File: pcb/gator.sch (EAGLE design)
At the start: 69 parts, among them J2 POWER_JACKPTH

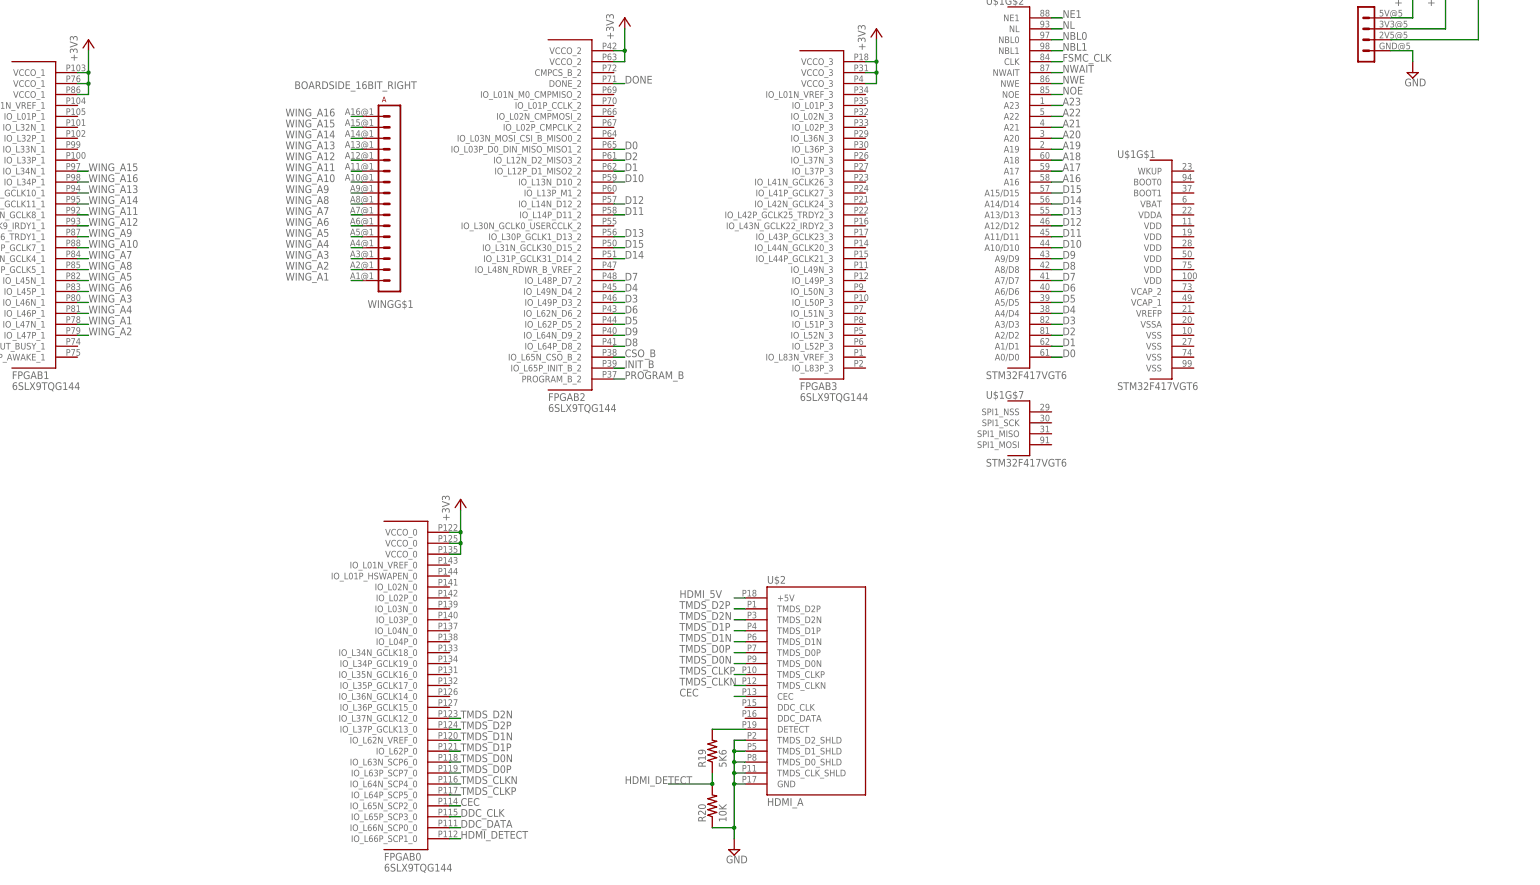
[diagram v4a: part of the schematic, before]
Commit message: Added SDRAM part and connected it to FPGA
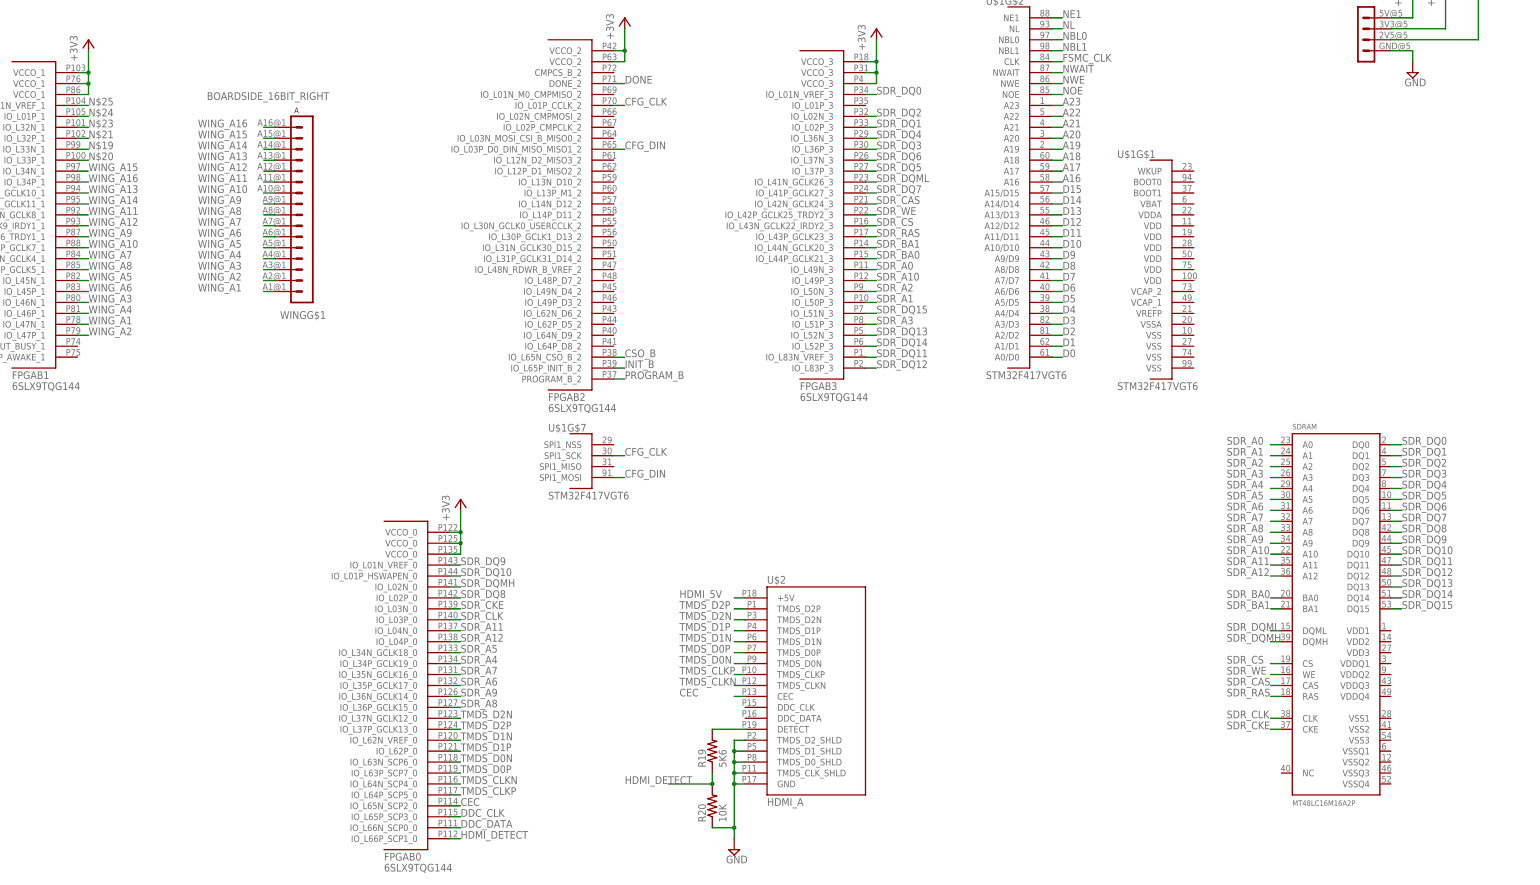
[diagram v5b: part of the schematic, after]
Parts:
- added SDRAM: MT48LC16M16A2P, gator:MT48LC16M16A2P
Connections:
- new net CFG_CLK: FPGAB2.IO_L01P_CCLK_2, U$1G$7.SPI1_SCK
- new net CFG_DIN: FPGAB2.IO_L03P_D0_DIN_MISO_MISO1_2, U$1G$7.SPI1_MOSI
- new net N$19: FPGAB1.IO_L33N_1
- new net N$20: FPGAB1.IO_L33P_1
- new net N$21: FPGAB1.IO_L32P_1
- new net N$23: FPGAB1.IO_L32N_1
- new net N$24: FPGAB1.IO_L01P_1
- new net N$25: FPGAB1.IO_L01N_VREF_1
- new net SDR_A0: FPGAB3.IO_L49N_3, SDRAM.A0
- new net SDR_A1: FPGAB3.IO_L50P_3, SDRAM.A1
- new net SDR_A10: FPGAB3.IO_L49P_3, SDRAM.A10
- new net SDR_A11: FPGAB0.IO_L04N_0, SDRAM.A11
- new net SDR_A12: FPGAB0.IO_L04P_0, SDRAM.A12
- new net SDR_A2: FPGAB3.IO_L50N_3, SDRAM.A2
- new net SDR_A3: FPGAB3.IO_L51P_3, SDRAM.A3
- new net SDR_A4: FPGAB0.IO_L34P_GCLK19_0, SDRAM.A4
- new net SDR_A5: FPGAB0.IO_L34N_GCLK18_0, SDRAM.A5
- new net SDR_A6: FPGAB0.IO_L35P_GCLK17_0, SDRAM.A6
- new net SDR_A7: FPGAB0.IO_L35N_GCLK16_0, SDRAM.A7
- new net SDR_A8: FPGAB0.IO_L36P_GCLK15_0, SDRAM.A8
- new net SDR_A9: FPGAB0.IO_L36N_GCLK14_0, SDRAM.A9
- new net SDR_BA0: FPGAB3.IO_L44P_GCLK21_3, SDRAM.BA0
- new net SDR_BA1: FPGAB3.IO_L44N_GCLK20_3, SDRAM.BA1
- new net SDR_CAS: FPGAB3.IO_L42N_GCLK24_3, SDRAM.CAS
- new net SDR_CKE: FPGAB0.IO_L03N_0, SDRAM.CKE
- new net SDR_CLK: FPGAB0.IO_L03P_0, SDRAM.CLK
- new net SDR_CS: FPGAB3.IO_L43N_GCLK22_IRDY2_3, SDRAM.CS
- new net SDR_DQ0: FPGAB3.IO_L01N_VREF_3, SDRAM.DQ0
- new net SDR_DQ1: FPGAB3.IO_L02P_3, SDRAM.DQ1
- new net SDR_DQ10: FPGAB0.IO_L01P_HSWAPEN_0, SDRAM.DQ10
- new net SDR_DQ11: FPGAB3.IO_L83N_VREF_3, SDRAM.DQ11
- new net SDR_DQ12: FPGAB3.IO_L83P_3, SDRAM.DQ12
- new net SDR_DQ13: FPGAB3.IO_L52N_3, SDRAM.DQ13
- new net SDR_DQ14: FPGAB3.IO_L52P_3, SDRAM.DQ14
- new net SDR_DQ15: FPGAB3.IO_L51N_3, SDRAM.DQ15
- new net SDR_DQ2: FPGAB3.IO_L02N_3, SDRAM.DQ2
- new net SDR_DQ3: FPGAB3.IO_L36P_3, SDRAM.DQ3
- new net SDR_DQ4: FPGAB3.IO_L36N_3, SDRAM.DQ4
- new net SDR_DQ5: FPGAB3.IO_L37P_3, SDRAM.DQ5
- new net SDR_DQ6: FPGAB3.IO_L37N_3, SDRAM.DQ6
- new net SDR_DQ7: FPGAB3.IO_L41P_GCLK27_3, SDRAM.DQ7
- new net SDR_DQ8: FPGAB0.IO_L02P_0, SDRAM.DQ8
- new net SDR_DQ9: FPGAB0.IO_L01N_VREF_0, SDRAM.DQ9
- new net SDR_DQMH: FPGAB0.IO_L02N_0, SDRAM.DQMH
- new net SDR_DQML: FPGAB3.IO_L41N_GCLK26_3, SDRAM.DQML
- new net SDR_RAS: FPGAB3.IO_L43P_GCLK23_3, SDRAM.RAS
- new net SDR_WE: FPGAB3.IO_L42P_GCLK25_TRDY2_3, SDRAM.WE
- net D0: no longer FPGAB2.IO_L03P_D0_DIN_MISO_MISO1_2
- net D1: no longer FPGAB2.IO_L12P_D1_MISO2_2
- net D10: no longer FPGAB2.IO_L13N_D10_2
- net D11: no longer FPGAB2.IO_L14P_D11_2
- net D12: no longer FPGAB2.IO_L14N_D12_2
- net D13: no longer FPGAB2.IO_L30P_GCLK1_D13_2
- net D14: no longer FPGAB2.IO_L31P_GCLK31_D14_2
- net D15: no longer FPGAB2.IO_L31N_GCLK30_D15_2
- net D2: no longer FPGAB2.IO_L12N_D2_MISO3_2
- net D3: no longer FPGAB2.IO_L49P_D3_2
- net D4: no longer FPGAB2.IO_L49N_D4_2
- net D5: no longer FPGAB2.IO_L62P_D5_2
- net D6: no longer FPGAB2.IO_L62N_D6_2
- net D7: no longer FPGAB2.IO_L48P_D7_2
- net D8: no longer FPGAB2.IO_L64P_D8_2
- net D9: no longer FPGAB2.IO_L64N_D9_2
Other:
- moved on the sheet: U$1G$7, WINGG$1

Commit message: Connected FSMC; 8-bit Papilio wing
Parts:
- removed WING: BOARDSIDE_16BIT_RIGHT, GadgetFactory_Pub:BOARDSIDE_16BIT_RIGHT
- added U$3: WING8, Papilio:WING8
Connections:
- removed net +5V: WINGG$2.5V, WINGG$3.5V
- removed net WING_A1: FPGAB1.IO_L47N_1, WINGG$1.A1
- removed net WING_A10: FPGAB1.IO_L42P_GCLK7_1, WINGG$1.A10
- removed net WING_A11: FPGAB1.IO_L41N_GCLK8_1, WINGG$1.A11
- removed net WING_A12: FPGAB1.IO_L41P_GCLK9_IRDY1_1, WINGG$1.A12
- removed net WING_A13: FPGAB1.IO_L40N_GCLK10_1, WINGG$1.A13
- removed net WING_A14: FPGAB1.IO_L40P_GCLK11_1, WINGG$1.A14
- removed net WING_A15: FPGAB1.IO_L34N_1, WINGG$1.A15
- removed net WING_A16: FPGAB1.IO_L34P_1, WINGG$1.A16
- removed net WING_A2: FPGAB1.IO_L47P_1, WINGG$1.A2
- removed net WING_A3: FPGAB1.IO_L46N_1, WINGG$1.A3
- removed net WING_A4: FPGAB1.IO_L46P_1, WINGG$1.A4
- removed net WING_A5: FPGAB1.IO_L45N_1, WINGG$1.A5
- removed net WING_A6: FPGAB1.IO_L45P_1, WINGG$1.A6
- removed net WING_A7: FPGAB1.IO_L43N_GCLK4_1, WINGG$1.A7
- removed net WING_A8: FPGAB1.IO_L43P_GCLK5_1, WINGG$1.A8
- removed net WING_A9: FPGAB1.IO_L42N_GCLK6_TRDY1_1, WINGG$1.A9
- new net N$26: FPGAB1.IO_L34N_1, U$3.1
- new net N$27: FPGAB1.IO_L34P_1, U$3.2
- net +3V3: no longer WINGG$2.3V3, WINGG$3.3V3
- net A16: now also FPGAB2.IO_L49P_D3_2
- net A17: now also FPGAB2.IO_L49N_D4_2
- net A18: now also FPGAB2.IO_L62P_D5_2
- net A19: now also FPGAB1.IO_L46P_1
- net A20: now also FPGAB1.IO_L46N_1
- net A21: now also FPGAB1.IO_L47P_1
- net A22: now also FPGAB1.IO_L47N_1
- net A23: now also FPGAB1.IO_L45N_1
- net D0: now also FPGAB2.IO_L62N_D6_2
- net D1: now also FPGAB2.IO_L64P_D8_2
- net D10: now also FPGAB2.IO_L30P_GCLK1_D13_2
- net D11: now also FPGAB2.IO_L30N_GCLK0_USERCCLK_2
- net D12: now also FPGAB2.IO_L31P_GCLK31_D14_2
- net D13: now also FPGAB2.IO_L31N_GCLK30_D15_2
- net D14: now also FPGAB2.IO_L48P_D7_2
- net D15: now also FPGAB2.IO_L48N_RDWR_B_VREF_2
- net D2: now also FPGAB1.IO_L40P_GCLK11_1
- net D3: now also FPGAB1.IO_L40N_GCLK10_1
- net D4: now also FPGAB2.IO_L12P_D1_MISO2_2
- net D5: now also FPGAB2.IO_L12N_D2_MISO3_2
- net D6: now also FPGAB2.IO_L13P_M1_2
- net D7: now also FPGAB2.IO_L13N_D10_2
- net D8: now also FPGAB2.IO_L14P_D11_2
- net D9: now also FPGAB2.IO_L14N_D12_2
- net GND: no longer WINGG$2.GND, WINGG$3.GND
- net INIT_B: no longer U$1G$9.PB0
- net N$19: now also FPGAB1.IO_L01N_VREF_1, U$3.7; no longer FPGAB1.IO_L33N_1
- net N$20: now also FPGAB1.IO_L01P_1, U$3.8; no longer FPGAB1.IO_L33P_1
- net N$21: now also FPGAB1.IO_L32N_1, U$3.5; no longer FPGAB1.IO_L32P_1
- net N$23: now also FPGAB1.IO_L32P_1, U$3.6; no longer FPGAB1.IO_L32N_1
- net N$24: now also FPGAB1.IO_L33N_1, U$3.3; no longer FPGAB1.IO_L01P_1
- net N$25: now also FPGAB1.IO_L33P_1, U$3.4; no longer FPGAB1.IO_L01N_VREF_1
- net NBL0: now also FPGAB1.IO_L43N_GCLK4_1
- net NBL1: now also FPGAB1.IO_L45P_1
- net NE1: now also FPGAB1.IO_L42N_GCLK6_TRDY1_1
- net NL: now also FPGAB1.IO_L43P_GCLK5_1
- net NOE: now also FPGAB1.IO_L41P_GCLK9_IRDY1_1
- net NWAIT: now also FPGAB1.IO_L42P_GCLK7_1
- net NWE: now also FPGAB1.IO_L41N_GCLK8_1
- net PROGRAM_B: no longer U$1G$9.PB1
- net VCC/2: no longer WINGG$2.2V5, WINGG$3.2V5

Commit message: Cleaned up power supplies and connected usb and micro sd
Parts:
- removed C18, C20: 100n, SparkFun-Passives:CAP0603-CAP
- removed C19: 2.2u, SparkFun-Passives:CAP0603-CAP
- removed TLV1117-25CDCYR: (no value), microbuilder:LM1117SOT223-REFLOW
- removed U$3: WING8, Papilio:WING8
- added R21, R22: 22, SparkFun-Passives:RESISTOR0603-RES
- added R23: 10K, SparkFun-Passives:RESISTOR0603-RES
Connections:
- removed net N$23: FPGAB1.IO_L32P_1, U$3.6
- removed net N$24: FPGAB1.IO_L33N_1, U$3.3
- removed net N$25: FPGAB1.IO_L33P_1, U$3.4
- removed net N$26: FPGAB1.IO_L34N_1, U$3.1
- removed net N$27: FPGAB1.IO_L34P_1, U$3.2
- removed net TCLK/SWCLK: JTAG.9
- removed net VCC/2: C19.1, C20.1, TLV1117-25CDCYR.OUT
- new net SPI_MISO: FPGAB2.IO_L02N_CMPMOSI_2, U$1G$7.SPI1_MISO
- net +3V3: now also SDRAM.VDD1, SDRAM.VDD2, SDRAM.VDD3, SDRAM.VDDQ1, SDRAM.VDDQ2, SDRAM.VDDQ3, SDRAM.VDDQ4
- net GND: now also SDRAM.VSS1, SDRAM.VSS2, SDRAM.VSS3, SDRAM.VSSQ1, SDRAM.VSSQ2, SDRAM.VSSQ3, SDRAM.VSSQ4, U$1G$1.VSS@10, U$1G$1.VSS@27, U$1G$1.VSS@74, U$1G$1.VSS@99, U$1G$1.VSSA; no longer C18.2, C19.2, C20.2, TLV1117-25CDCYR.ADJ
- net N$1: now also R21.2; no longer USBA.D+
- net N$19: now also R21.1, USBA.D+; no longer FPGAB1.IO_L01N_VREF_1, U$3.7
- net N$2: now also R22.2; no longer USBA.D-
- net N$20: now also R22.1, USBA.D-; no longer FPGAB1.IO_L01P_1, U$3.8
- net N$21: now also MIC5219-5.0YM1.EN, R23.1; no longer FPGAB1.IO_L32N_1, U$3.5
- net TCK/SWCLK: now also JTAG.9
- net USB_EN: no longer MIC5219-5.0YM1.EN
- net V+: now also R23.2; no longer C18.1, TLV1117-25CDCYR.IN
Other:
- moved on the sheet: U$1G$9

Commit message: Added HDMI termination, oscillators, improved routing
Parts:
- added C18, C19: 20p, SparkFun-Passives:CAP0603-CAP
- added OSC_50M: OSCILLATOR5X3-PIN1-INDICATED, SparkFun-FreqCtrl:OSCILLATOR5X3-PIN1-INDICATED
- added R24, R25: 10K, SparkFun-Passives:RESISTOR0603-RES
- added R26: 2K2, SparkFun-Passives:RESISTOR0603-RES
- added R27, R28: 51, SparkFun-Passives:RESISTOR-ARRAY0603-ARV
- added Y1: 12MHz, SparkFun-FreqCtrl:CRYSTALHC49US
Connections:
- new net FPGA_CLK1: FPGAB1.IO_L34N_1, U$1G$8.MCO1
- new net FPGA_CLK2: FPGAB1.IO_L34P_1
- new net N$29: C18.1, U$1G$8.OSC_IN, Y1.2
- new net N$30: C19.1, U$1G$8.OSC_OUT, Y1.1
- new net N$31: OSC_50M.EN, R26.1
- new net SD_DETECT: MICROSD.SHIELD@2, R24.1, U$1G$9.PC7
- net +3V3: now also OSC_50M.VCC, R24.2, R26.2; no longer FPGAB0.VCCO_0@000, FPGAB0.VCCO_0@001, FPGAB0.VCCO_0@002, FPGAB1.VCCO_1@000, FPGAB1.VCCO_1@001, FPGAB1.VCCO_1@002, FPGAB2.VCCO_2@000, FPGAB2.VCCO_2@001, FPGAB3.VCCO_3@000, FPGAB3.VCCO_3@001, FPGAB3.VCCO_3@002, FPGABVCCAUX.VCCAUX@000, FPGABVCCAUX.VCCAUX@001, FPGABVCCAUX.VCCAUX@002, FPGABVCCAUX.VCCAUX@003, FPGABVCCAUX.VCCAUX@004
- net 50MHZ_OSC: now also OSC_50M.OUT
- net GND: now also C18.2, C19.2, OSC_50M.GND
- net TMDS_CLKN: now also R27A.1
- net TMDS_CLKP: now also R27B.1
- net TMDS_D0N: now also R27C.1
- net TMDS_D0P: now also R27D.1
- net TMDS_D1N: now also R28A.1
- net TMDS_D1P: now also R28B.1
- net TMDS_D2N: now also R28C.1
- net TMDS_D2P: now also R28D.1
- net USB_EN: now also R25.1, U$1G$9.PC6; no longer U$1G$5.USB_EN_ID
- net V+: now also R25.2
- net VCCIO: now also FPGAB0.VCCO_0@000, FPGAB0.VCCO_0@001, FPGAB0.VCCO_0@002, FPGAB1.VCCO_1@000, FPGAB1.VCCO_1@001, FPGAB1.VCCO_1@002, FPGAB2.VCCO_2@000, FPGAB2.VCCO_2@001, FPGAB3.VCCO_3@000, FPGAB3.VCCO_3@001, FPGAB3.VCCO_3@002, FPGABVCCAUX.VCCAUX@000, FPGABVCCAUX.VCCAUX@001, FPGABVCCAUX.VCCAUX@002, FPGABVCCAUX.VCCAUX@003, FPGABVCCAUX.VCCAUX@004, R27A.2, R27B.2, R27C.2, R27D.2, R28A.2, R28B.2, R28C.2, R28D.2
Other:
- note added: "PLL: M=6, N=168, P=2, Q=7"
- moved on the sheet: U$1G$8
